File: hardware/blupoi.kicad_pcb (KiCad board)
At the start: 2 copper layers, 505.1 x 22.2 mm, 204 parts, among them P1 MICRO-B-USB, SW1 PM_BTN, U1 NRF52832, U2 TPS63031DSKR, U3 bno055, U4 ics43432, U5 BQ24075RGTT, U6 MAX16054AZT+T, X1 32MHz

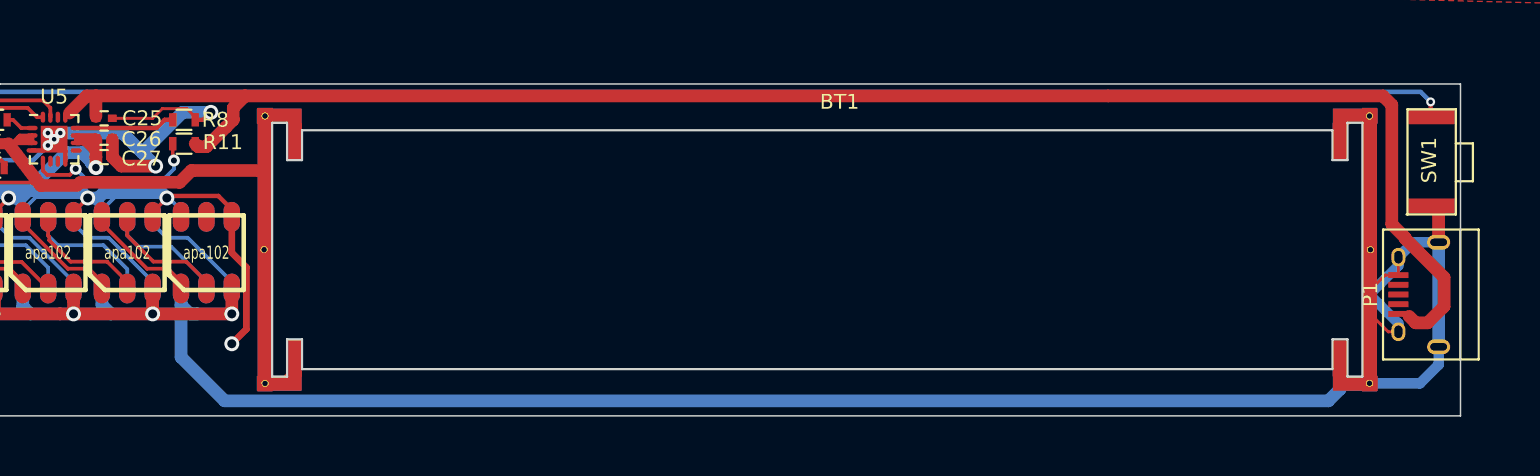
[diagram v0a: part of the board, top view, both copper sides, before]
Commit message: Made trace nicer
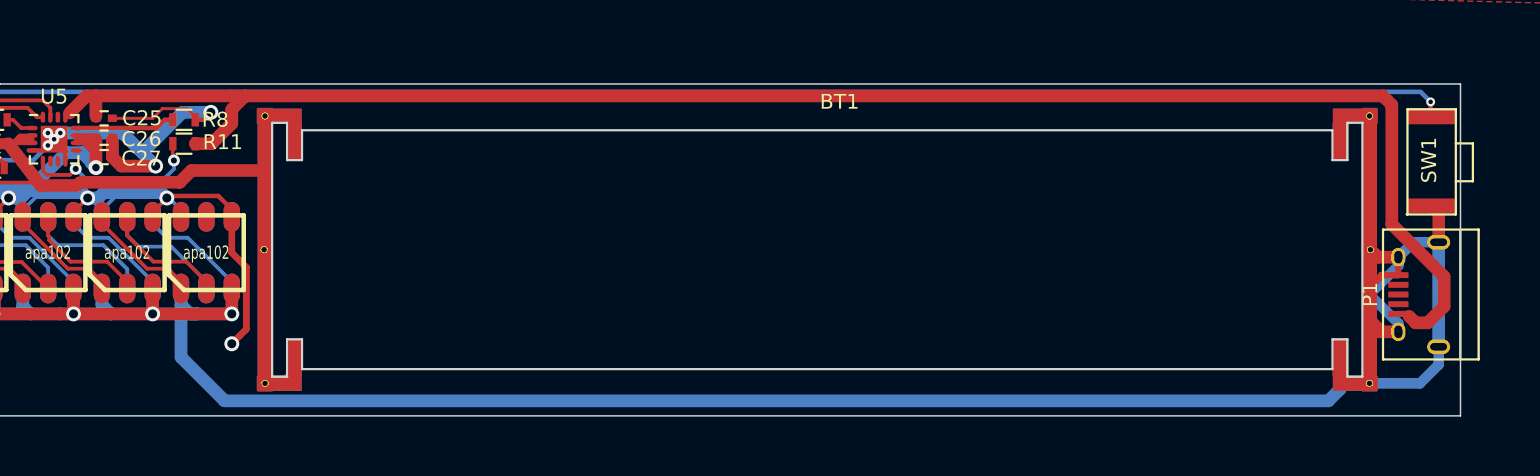
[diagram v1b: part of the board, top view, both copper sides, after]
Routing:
- net GND: track 1895.4 -> 1913.3 mm
- net VUSB: track 114.6 -> 115.3 mm
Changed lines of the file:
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@@
   (general
     (links 799)
-    (no_connects 26)
+    (no_connects 25)
     (area -67.365001 99.149999 437.850001 121.480001)
     (thickness 1.6)
     (drawings 13)
-    (tracks 3755)
+    (tracks 3762)
     (zones 0)
     (modules 204)
@@
   )
   (setup
-    (last_trace_width 0.2)
+    (last_trace_width 0.85)
     (user_trace_width 0.2)
     (user_trace_width 0.25)
@@
     (pad_to_mask_clearance 0.2)
     (aux_axis_origin 0 0)
-    (grid_origin 138.2 113)
     (visible_elements FFFFFF7F)
     (pcbplotparams
@@
   (segment (start -33.75 120) (end -33.3 120) (width 0.2) (layer F.Cu) (net 1))
   (segment (start -34.300001 120.550001) (end -33.75 120) (width 0.2) (layer F.Cu) (net 1))
+  (segment (start 433.63746 112.0009) (end 432.51246 112.0009) (width 0.45) (layer F.Cu) (net 2))
+  (segment (start 432.51246 112.0009) (end 431.7045 112.80886) (width 0.45) (layer F.Cu) (net 2))
+  (segment (start 431.7045 112.80886) (end 431.7045 118.899947) (width 0.45) (layer F.Cu) (net 2))
+  (segment (start 431.7045 118.899947) (end 431.7045 119.2535) (width 0.45) (layer F.Cu) (net 2))
+  (segment (start 433.63746 112.0009) (end 433.63746 110.8009) (width 0.4) (layer F.Cu) (net 2))
+  (segment (start 433.63746 115.8009) (end 432.31246 115.8009) (width 0.85) (layer F.Cu) (net 2))
+  (segment (start 432.31246 115.8009) (end 431.7045 115.19294) (width 0.85) (layer F.Cu) (net 2))
+  (segment (start 431.7045 115.19294) (end 431.7045 110.3) (width 0.85) (layer F.Cu) (net 2))
+  (segment (start 433.63746 110.8009) (end 432.2689 110.8009) (width 0.85) (layer F.Cu) (net 2))
+  (segment (start 432.2689 110.8009) (end 431.768 110.3) (width 0.85) (layer F.Cu) (net 2))
   (segment (start -10.712832 114.412832) (end -10.525664 114.6) (width 0.45) (layer F.Cu) (net 2))
   (segment (start -10.525664 114.6) (end -10.2 114.6) (width 0.45) (layer F.Cu) (net 2))
@@
   (segment (start 431.768 114.60644) (end 431.768 113.653553) (width 0.2) (layer F.Cu) (net 2))
   (segment (start 431.768 113.653553) (end 431.768 113.3) (width 0.2) (layer F.Cu) (net 2))
-  (segment (start 433.63746 110.8009) (end 433.63746 112.0009) (width 0.2) (layer F.Cu) (net 2))
   (segment (start -6.7 119.35) (end -7.075 118.975) (width 0.4) (layer F.Cu) (net 2))
   (segment (start -7.075 118.975) (end -7.85 118.975) (width 0.4) (layer F.Cu) (net 2))
@@
   (segment (start -8.55 118.3) (end -7.85 118.3) (width 0.4) (layer F.Cu) (net 328))
   (segment (start -8.550001 119.624999) (end -8.55 118.3) (width 0.4) (layer F.Cu) (net 328))
-  (segment (start 434.36253 114.76253) (end 434.8 115.2) (width 0.85) (layer F.Cu) (net 329))
-  (segment (start 414.2 100) (end 356.4 100) (width 0.85) (layer F.Cu) (net 329))
-  (segment (start 434.8 115.2) (end 435.6 115.2) (width 0.85) (layer F.Cu) (net 329))
-  (segment (start 435.6 115.2) (end 436.7 114.1) (width 0.85) (layer F.Cu) (net 329))
-  (segment (start 434.093099 109.493099) (end 433.2 108.6) (width 0.85) (layer F.Cu) (net 329))
-  (segment (start 436.7 114.1) (end 436.7 112.157791) (width 0.85) (layer F.Cu) (net 329))
-  (segment (start 436.7 112.157791) (end 434.093099 109.55089) (width 0.85) (layer F.Cu) (net 329))
-  (segment (start 433.2 100.6) (end 432.6 100) (width 0.85) (layer F.Cu) (net 329))
-  (segment (start 434.093099 109.55089) (end 434.093099 109.493099) (width 0.85) (layer F.Cu) (net 329))
-  (segment (start 433.2 108.6) (end 433.2 100.6) (width 0.85) (layer F.Cu) (net 329))
-  (segment (start 432.6 100) (end 414.2 100) (width 0.85) (layer F.Cu) (net 329))
+  (segment (start 356.4 100) (end 432.6 100) (width 0.85) (layer F.Cu) (net 329))
+  (segment (start 432.6 100) (end 433.2 100.6) (width 0.85) (layer F.Cu) (net 329))
+  (segment (start 436.7 112.1) (end 436.7 114.1) (width 0.85) (layer F.Cu) (net 329))
+  (segment (start 436.7 114.1) (end 435.6 115.2) (width 0.85) (layer F.Cu) (net 329))
+  (segment (start 433.2 100.6) (end 433.2 108.6) (width 0.85) (layer F.Cu) (net 329))
+  (segment (start 433.2 108.6) (end 436.7 112.1) (width 0.85) (layer F.Cu) (net 329))
+  (segment (start 435.6 115.2) (end 434.8 115.2) (width 0.85) (layer F.Cu) (net 329))
+  (segment (start 434.8 115.2) (end 434.36253 114.76253) (width 0.85) (layer F.Cu) (net 329))
+  (segment (start 433.63746 114.6009) (end 434.2009 114.6009) (width 0.4) (layer F.Cu) (net 329))
+  (segment (start 434.2009 114.6009) (end 434.36253 114.76253) (width 0.4) (layer F.Cu) (net 329))
+  (segment (start 355.5 101.85) (end 355.5 100.9) (width 0.85) (layer F.Cu) (net 329))
+  (segment (start 355.5 100.9) (end 356.4 100) (width 0.85) (layer F.Cu) (net 329))
+  (segment (start 356.4 100) (end 355.5 100) (width 0.85) (layer F.Cu) (net 329))
+  (segment (start 355.5 100) (end 346.4 100) (width 0.85) (layer F.Cu) (net 329))
+  (segment (start 353.05 103.2) (end 354.15 103.2) (width 0.85) (layer F.Cu) (net 329))
+  (segment (start 354.15 103.2) (end 355.5 101.85) (width 0.85) (layer F.Cu) (net 329))
   (segment (start 346.4 100) (end 345.775 100) (width 0.85) (layer F.Cu) (net 329))
-  (segment (start 356.4 100) (end 346.4 100) (width 0.85) (layer F.Cu) (net 329))
   (segment (start 346.4 100) (end 346.4 101.37499) (width 0.85) (layer F.Cu) (net 329))
   (segment (start 345.775 100) (end 344.62501 101.14999) (width 0.85) (layer F.Cu) (net 329))
-  (segment (start 353.8 103.4) (end 353.25 103.4) (width 0.85) (layer F.Cu) (net 329))
-  (segment (start 353.25 103.4) (end 353.05 103.2) (width 0.85) (layer F.Cu) (net 329))
-  (segment (start 355.1 102.1) (end 353.8 103.4) (width 0.85) (layer F.Cu) (net 329))
-  (segment (start 355.1 102.1) (end 355.599999 101.600001) (width 0.85) (layer F.Cu) (net 329))
-  (segment (start 355.599999 101.600001) (end 355.599999 100.800001) (width 0.85) (layer F.Cu) (net 329))
-  (segment (start 355.599999 100.800001) (end 356.4 100) (width 0.85) (layer F.Cu) (net 329))
   (segment (start 346.45 101.5) (end 346.4 101.5) (width 0.25) (layer F.Cu) (net 329))
   (segment (start 353.05 103.4) (end 353.05 103.2) (width 0.3) (layer F.Cu) (net 329))

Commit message: Renamed battery holder to BAT
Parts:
- renumbered BT1 to BAT
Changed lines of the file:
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@@
   (module 16650_holder:16650_in_pcb_socket (layer F.Cu)
     (at 396.208 102.299)
-    (fp_text reference BT1 (at 0 -1.905) (layer F.SilkS)
+    (fp_text reference BAT (at -0.008 -1.299) (layer F.SilkS)
       (effects (font (size 1 1) (thickness 0.15)))
     )

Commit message: hw_0.1
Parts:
- added G***: LOGO, memcpy_logo:memcpy_logo_20x5.5mm, B.Cu at (339.5, 117.8)
- added G***: LOGO, open_source_hardware:open_source_hardware_7x5mm, B.Cu at (326.2, 118.0)
- added G***: LOGO, memcpy_logo:memcpy_logo_20x5.5mm, F.Cu at (339.5, 117.8)
- added G***: LOGO, open_source_hardware:open_source_hardware_7x5mm, F.Cu at (326.2, 117.6)
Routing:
- net GND: track 1913.3 -> 1928.8 mm
- net VUSB: track 115.3 -> 117.8 mm
- net MIC_I2S_SD: track 58.8 -> 59.3 mm
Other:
- rule via_min_size: 0.4 -> 0.3
- board text added: "0.1"

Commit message: Updated HW
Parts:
- G*** (x2): footprint open_source_hardware:open_source_hardware_7x5mm -> open_source_hardware:open_source_hardware_6.7x6
- G*** (x2): footprint memcpy_logo:memcpy_logo_20x5.5mm -> memcpy_logo:memcpy_logo_24.2x6.7mm
- moved G*** 1.43 mm to (324.8, 117.3)
- moved G*** 1.40 mm to (324.8, 118.0)
- moved G*** 0.92 mm to (340.4, 117.6) (x2)
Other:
- board text added: "0.2"
- board text removed: "0.1"

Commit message: Add +/- and add missing copper pads
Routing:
- net VIN: track 996.2 -> 991.7 mm
- net PM_EN2: track 12.1 -> 12.9 mm
- removed copper zone on B.Cu, net GND
- removed copper zone on F.Cu, net VIN

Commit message: Removed ALL tracks
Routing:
- net GND: track 1928.8 -> 0.00 mm, vias 97 -> 0
- net VIN: track 991.7 -> 0.00 mm, vias 77 -> 0
- net V3.3: track 319.2 -> 0.00 mm, vias 10 -> 0
- net ACC_I2C_SCL: track 251.7 -> 0.00 mm, vias 2 -> 0
- net ACC_I2C_SDA: track 250.8 -> 0.00 mm, vias 4 -> 0
- net (no net): track 130.9 -> 0.00 mm
- net VUSB: track 118.0 -> 0.00 mm
- net PM_SWITCH: track 110.4 -> 0.00 mm, vias 2 -> 0
- net RX: track 70.0 -> 0.00 mm, vias 2 -> 0
- net TX: track 68.4 -> 0.00 mm, vias 2 -> 0
- net MIC_I2S_SD: track 59.3 -> 0.00 mm, vias 7 -> 0
- net MIC_I2S_WS: track 51.2 -> 0.00 mm, vias 2 -> 0
- net VBAT: track 50.8 -> 0.00 mm, vias 2 -> 0
- net MIC_I2S_SCK: track 50.8 -> 0.00 mm
- net RESET: track 41.4 -> 0.00 mm, vias 1 -> 0
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
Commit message: Increase MIC hole size
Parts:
- L2: footprint Capacitors_SMD:C_0603 -> Inductors_NEOSID:Neosid_Inductor_SM1206
- moved L2 0.52 mm to (36.3, 117.6)
